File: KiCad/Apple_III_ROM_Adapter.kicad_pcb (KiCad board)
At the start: 2 copper layers, 20.8 x 57.4 mm, 5 parts, among them U1 2532, U2 2764

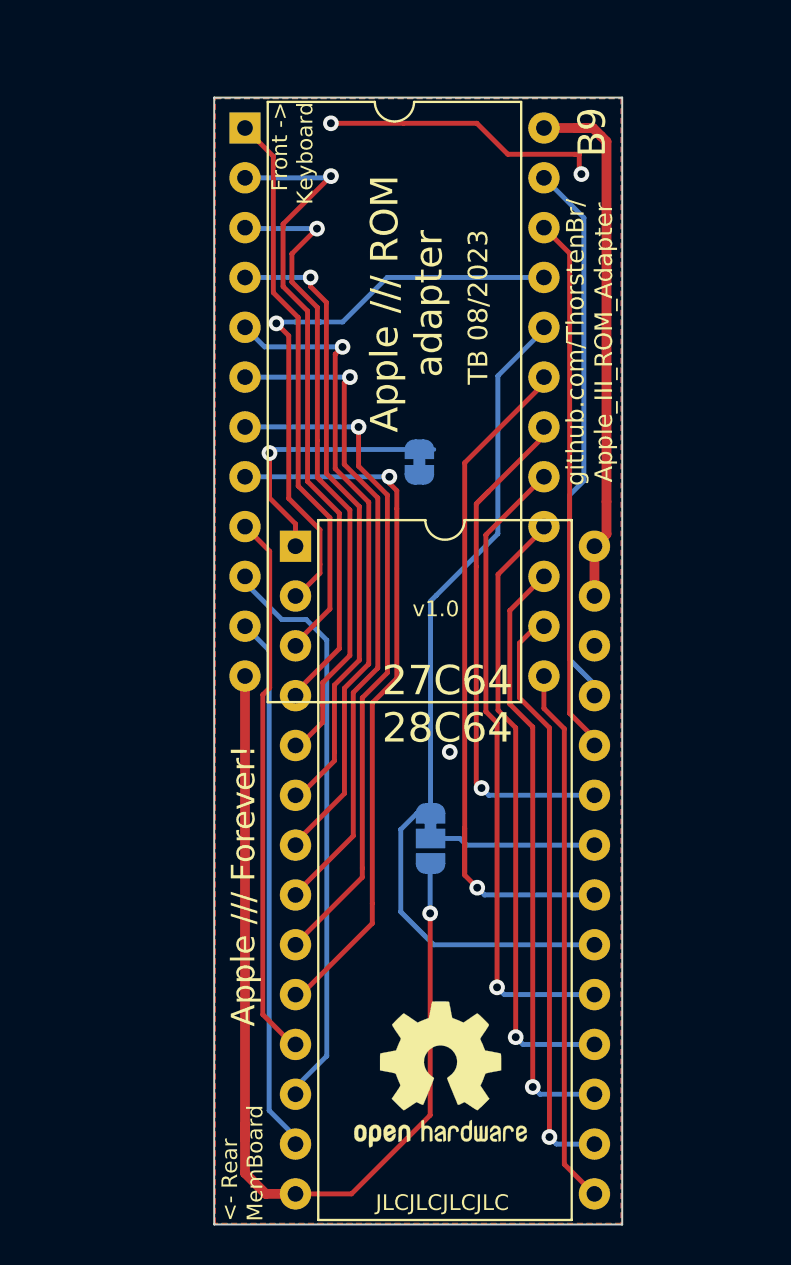
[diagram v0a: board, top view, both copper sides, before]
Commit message: New PCB design, v2.0 EPROM rotated by 90 degrees, moved all the way back to align with the memory sandwich board.
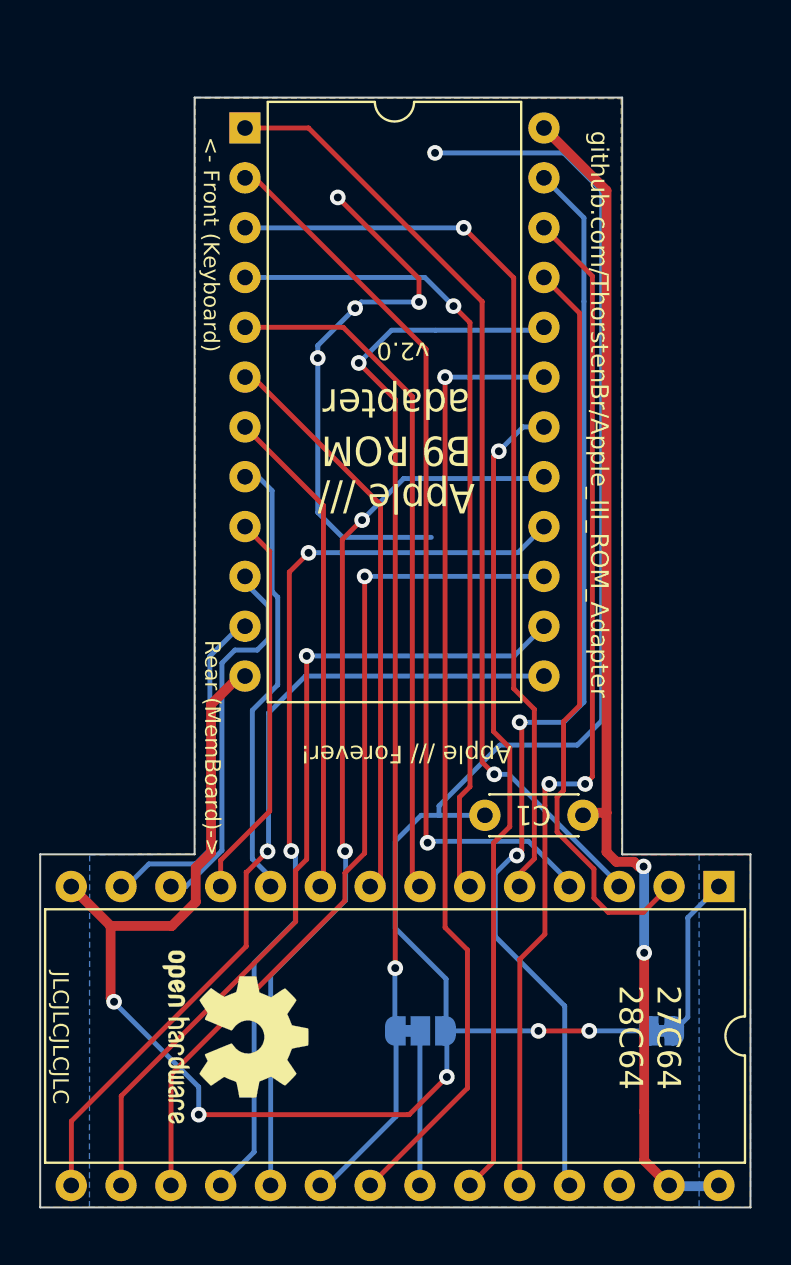
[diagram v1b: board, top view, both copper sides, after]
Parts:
- added C1: 100nF, Capacitor_THT:C_Disc_D4.3mm_W1.9mm_P5.00mm, F.Cu at (143.2, 93.7)
- moved JP2 31.5 mm to (147.2, 104.7), turned to 180 degrees
- moved U2 27.7 mm to (150.1, 97.3), turned to -90 degrees
- moved REF*** 10.6 mm to (125.5, 105.0), turned to -90 degrees
- moved JP1 9.82 mm to (134.9, 104.7), turned to 0 degrees
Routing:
- net GND: track 65.2 -> 148.8 mm, vias 4 -> 10
- net VCC: track 27.7 -> 60.7 mm, vias 0 -> 2
- net /A8: track 27.7 -> 57.5 mm, vias 0 -> 2
- net /A9: track 27.1 -> 53.1 mm, vias 0 -> 2
- net /A7: track 28.9 -> 48.8 mm, vias 0 -> 1
- net /D3: track 27.5 -> 43.8 mm, vias 0 -> 1
- net /D6: track 31.5 -> 46.9 mm, vias 1 -> 2
- net /A11: track 26.6 -> 41.5 mm
- net /D4: track 29.9 -> 44.3 mm
- net /D5: track 30.5 -> 45.0 mm
- net /D7: track 32.6 -> 46.9 mm, vias 1 -> 2
- net /A5: track 33.0 -> 46.5 mm
- net /A0: track 35.9 -> 22.9 mm, vias 1 -> 0
- net /A6: track 33.8 -> 46.4 mm
- net /A10: track 36.4 -> 48.8 mm
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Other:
- board size 20.8 x 57.4 mm -> 36.2 x 56.6 mm
- board text added: "<- Front (Keyboard)"
- board text added: "Apple /// B9 ROM adapter"
- board text added: "CC-BY-SA 4.0"
- board text added: "CS1|A12"
- board text added: "NC"
- board text added: "Rear (MemBoard)->"
- board text added: "TCB 10/2023"
- board text added: "github.com/ThorstenBr/Apple_III_ROM_Adapter"
- board text added: "v2.0"
- board text removed: "<- Rear MemBoard"
- board text removed: "Apple /// ROM adapter"
- board text removed: "B9"
- board text removed: "CS1"
- board text removed: "Front -> Keyboard"
- board text removed: "TB 08/2023"
- board text removed: "github.com/ThorstenBr/ Apple_III_ROM_Adapter"
- board text removed: "v1.0"
